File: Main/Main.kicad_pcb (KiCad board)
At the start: 2 copper layers, 55 parts, among them J1 Conn_02x16_Odd_Even, J2 TYPE-C 6P, Q3 S9013 J3(RANGE:200-350), U1 BQ24074RGT, U2 DRV8833PW, U3 HUSB237-AA001-DN06R, U4 RT9742GGJ5, U5 RT9742GGJ5, U6 INA219AxDCN, U7 TPS63802DLAR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

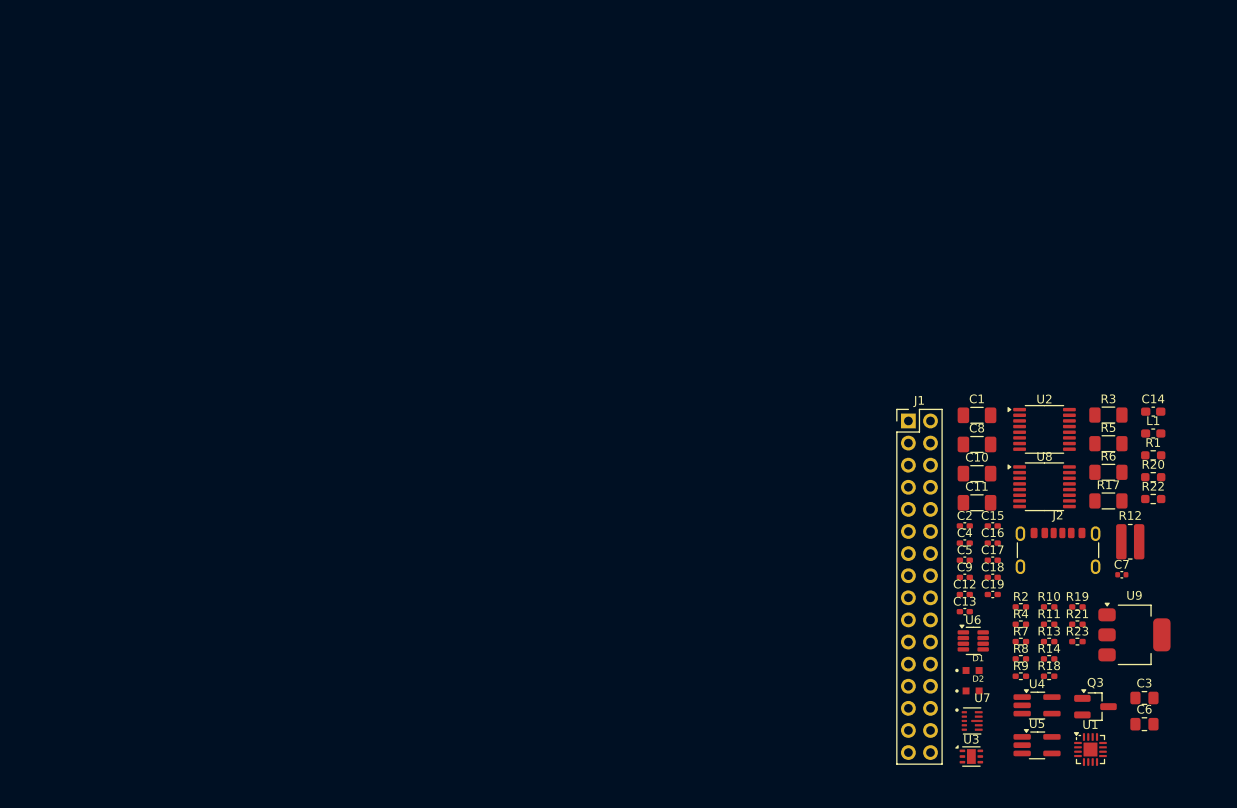
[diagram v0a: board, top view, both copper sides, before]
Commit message: Started PCB and Started Adding test points
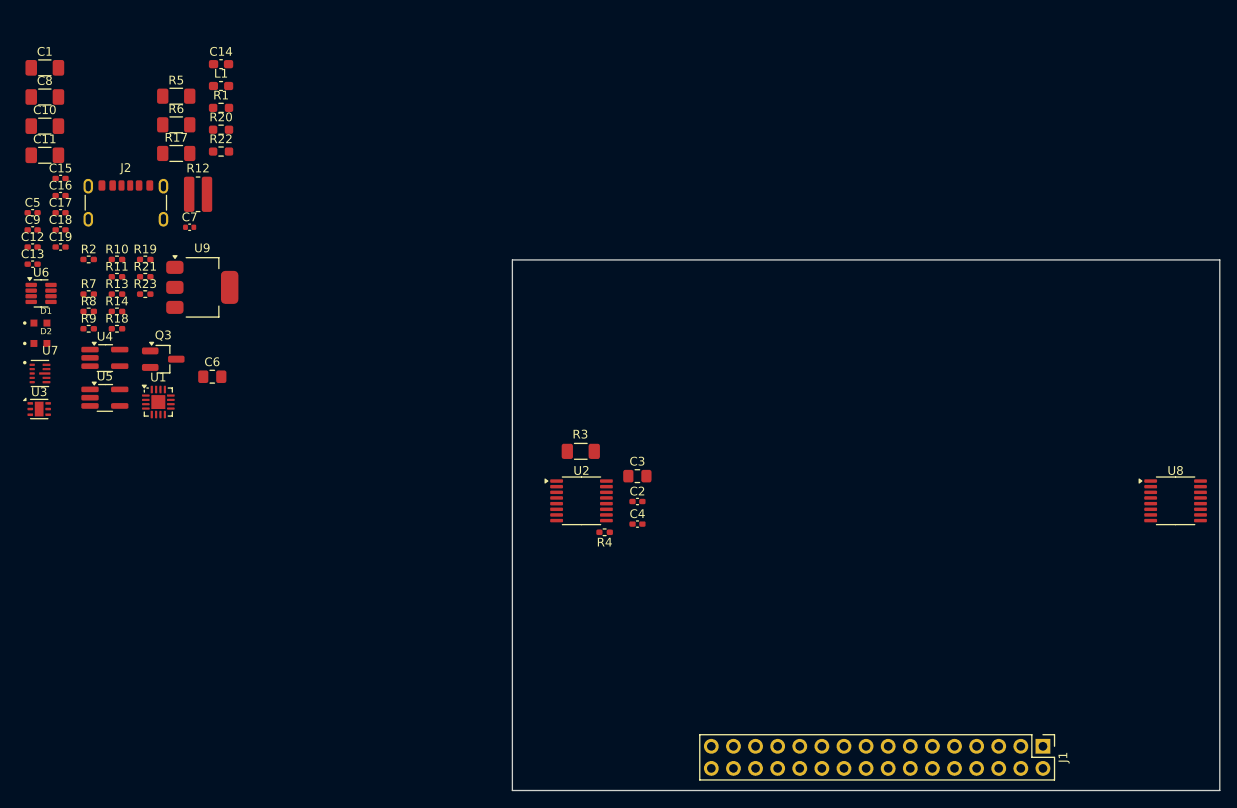
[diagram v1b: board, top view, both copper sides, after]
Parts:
- moved C1 114.3 mm to (40.3, 28.7)
- moved C10 114.3 mm to (40.3, 35.4)
- moved C11 114.3 mm to (40.3, 38.8)
- moved C14 114.3 mm to (60.5, 28.3)
- moved C15 114.3 mm to (42.1, 41.4)
- moved C16 114.3 mm to (42.1, 43.4)
- moved C17 114.3 mm to (42.1, 45.4)
- moved C18 114.3 mm to (42.1, 47.3)
- moved C19 114.3 mm to (42.1, 49.3)
- moved C8 114.3 mm to (40.3, 32.1)
- moved J2 114.3 mm to (49.6, 45.3)
- moved L1 114.3 mm to (60.5, 30.8)
- moved R1 114.3 mm to (60.5, 33.3)
- moved R20 114.3 mm to (60.5, 35.8)
- moved R22 114.3 mm to (60.5, 38.3)
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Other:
- board outline added: 81.3 x 61 mm

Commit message: connected first motor control
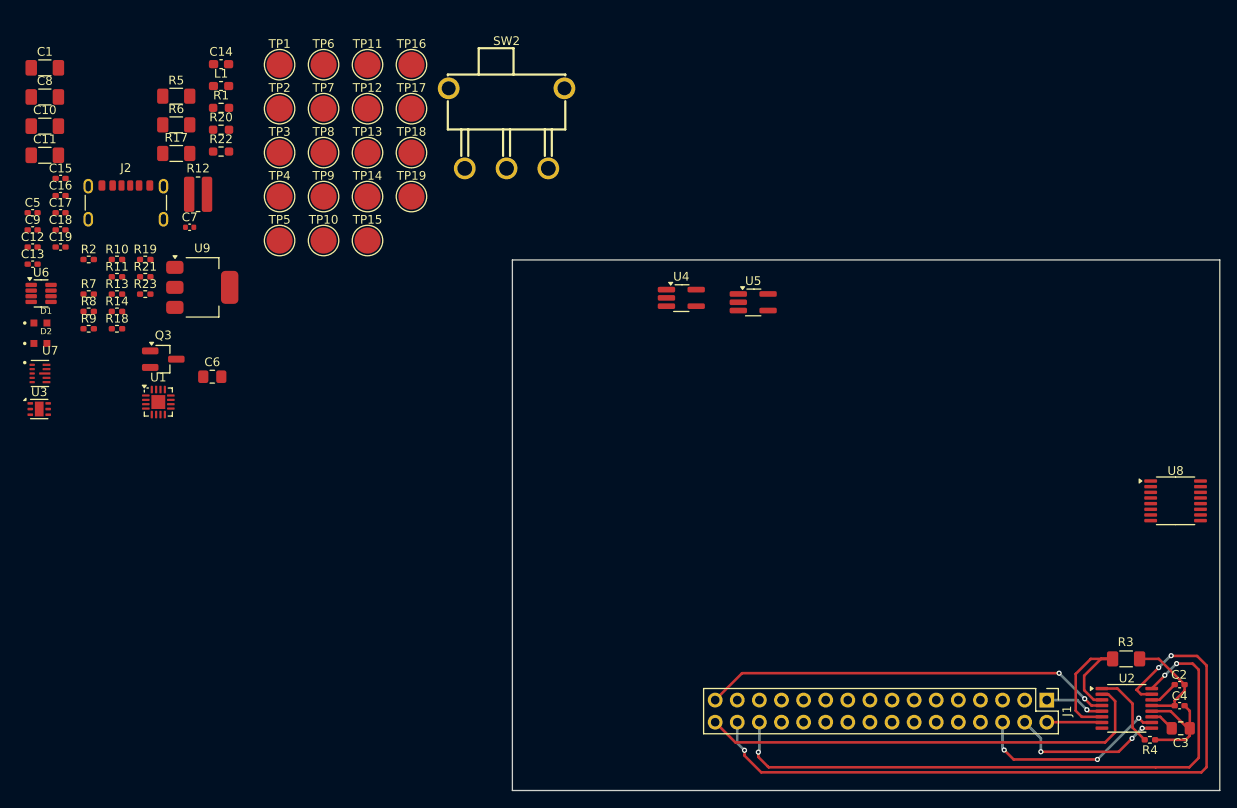
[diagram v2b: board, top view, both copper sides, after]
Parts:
- added SW2: SS-12D11G3R, SS-12D11G3R:SW-TH_SS-12D11L3, F.Cu at (93.3, 35.7)
- added TP1: TestPoint, TestPoint:TestPoint_Pad_D3.0mm, F.Cu at (67.2, 28.4)
- added TP10: TestPoint, TestPoint:TestPoint_Pad_D3.0mm, F.Cu at (72.3, 48.6)
- added TP11: TestPoint, TestPoint:TestPoint_Pad_D3.0mm, F.Cu at (77.3, 28.4)
- added TP12: TestPoint, TestPoint:TestPoint_Pad_D3.0mm, F.Cu at (77.3, 33.4)
- added TP13: TestPoint, TestPoint:TestPoint_Pad_D3.0mm, F.Cu at (77.3, 38.5)
- added TP14: TestPoint, TestPoint:TestPoint_Pad_D3.0mm, F.Cu at (77.3, 43.5)
- added TP15: TestPoint, TestPoint:TestPoint_Pad_D3.0mm, F.Cu at (77.3, 48.6)
- added TP16: TestPoint, TestPoint:TestPoint_Pad_D3.0mm, F.Cu at (82.4, 28.4)
- added TP17: TestPoint, TestPoint:TestPoint_Pad_D3.0mm, F.Cu at (82.4, 33.4)
- added TP18: TestPoint, TestPoint:TestPoint_Pad_D3.0mm, F.Cu at (82.4, 38.5)
- added TP19: TestPoint, TestPoint:TestPoint_Pad_D3.0mm, F.Cu at (82.4, 43.5)
- added TP2: TestPoint, TestPoint:TestPoint_Pad_D3.0mm, F.Cu at (67.2, 33.4)
- added TP3: TestPoint, TestPoint:TestPoint_Pad_D3.0mm, F.Cu at (67.2, 38.5)
- added TP4: TestPoint, TestPoint:TestPoint_Pad_D3.0mm, F.Cu at (67.2, 43.5)
- added TP5: TestPoint, TestPoint:TestPoint_Pad_D3.0mm, F.Cu at (67.2, 48.6)
- added TP6: TestPoint, TestPoint:TestPoint_Pad_D3.0mm, F.Cu at (72.3, 28.4)
- added TP7: TestPoint, TestPoint:TestPoint_Pad_D3.0mm, F.Cu at (72.3, 33.4)
- added TP8: TestPoint, TestPoint:TestPoint_Pad_D3.0mm, F.Cu at (72.3, 38.5)
- added TP9: TestPoint, TestPoint:TestPoint_Pad_D3.0mm, F.Cu at (72.3, 43.5)
- moved U5 75.3 mm to (121.7, 55.7)
- moved C3 68.8 mm to (170.8, 104.6), turned to 180 degrees
- moved U2 67.0 mm to (164.6, 102.3)
- moved R3 67.0 mm to (164.5, 96.6)
- moved R4 67.0 mm to (167.2, 105.9)
- moved U4 66.6 mm to (113.4, 55.2)
- moved C2 65.7 mm to (170.6, 99.6), turned to 180 degrees
- moved C4 65.7 mm to (170.6, 102.0), turned to 180 degrees
- moved J1 5.33 mm to (155.4, 101.4)
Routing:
- net /MOTOR1_CTRL2: track 0.00 -> 82.2 mm, vias 0 -> 3
- net /MOTOR1_CTRL1: track 0.00 -> 72.6 mm, vias 0 -> 3
- net /MOTOR1_A_OUT: track 0.00 -> 52.8 mm
- net /MOTOR1_B_OUT: track 0.00 -> 47.4 mm, vias 0 -> 2
- net /MOTOR2_CTRL2: track 0.00 -> 23.0 mm, vias 0 -> 3
- net Net-(U2-AISEN): track 0.00 -> 20.7 mm
- net /MOTOR2_CTRL1: track 0.00 -> 18.1 mm, vias 0 -> 3
- net /3V3 Out: track 0.00 -> 13.1 mm
- net GND: track 0.00 -> 12.0 mm
- net Net-(U2-~{SLEEP}): track 0.00 -> 8.98 mm
- net /Motor2_B_OUT: track 0.00 -> 6.86 mm, vias 0 -> 1
- net /Motor2_A_OUT: track 0.00 -> 6.35 mm
- net Net-(U2-VINT): track 0.00 -> 3.36 mm
- net Net-(U2-VCP): track 0.00 -> 2.84 mm

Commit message: Completed substantial PCB Connections
Completed: 1A Switching, Charging IC
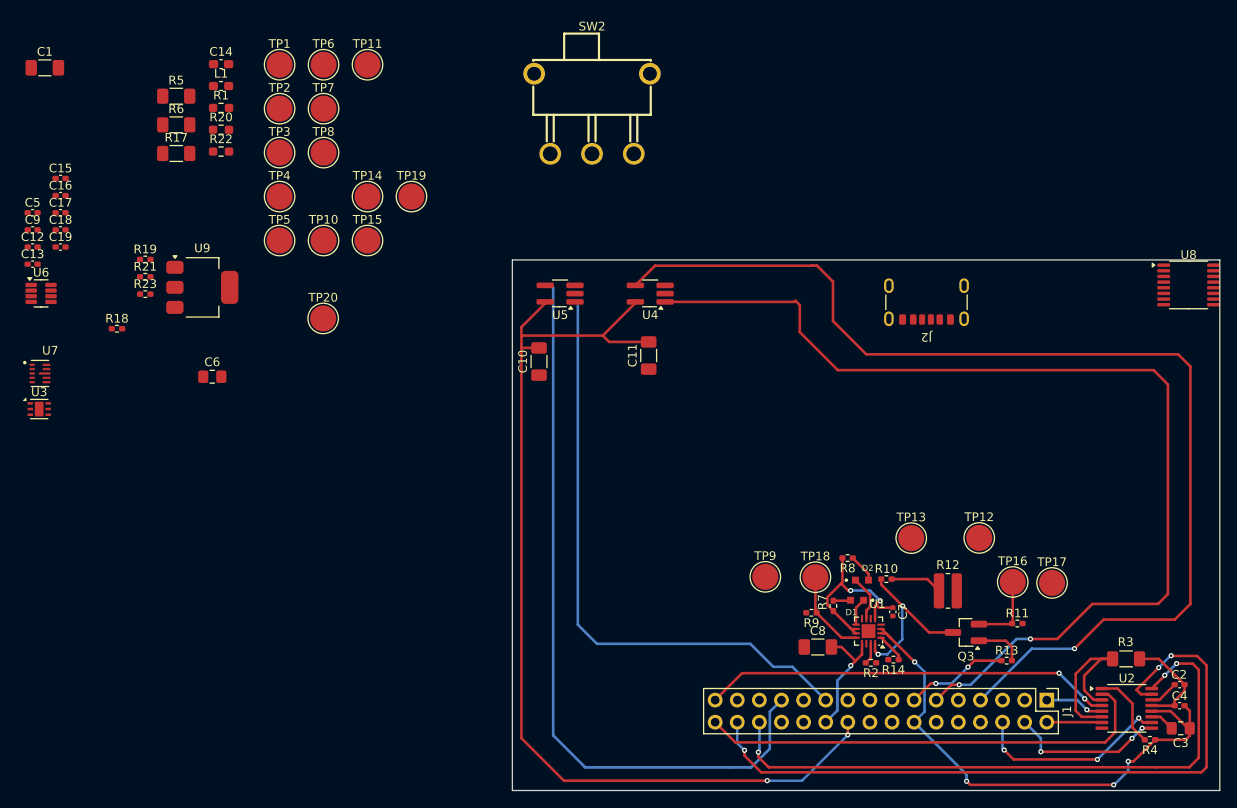
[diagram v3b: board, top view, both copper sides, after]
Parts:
- added TP20: TestPoint, TestPoint:TestPoint_Pad_D3.0mm, F.Cu at (72.2, 57.5)
- moved R11 110.9 mm to (152.0, 92.6)
- moved R13 110.6 mm to (150.8, 96.8)
- moved C8 109.0 mm to (129.1, 95.3)
- moved R2 101.1 mm to (135.2, 97.1), turned to 180 degrees
- moved D1 99.1 mm to (133.6, 89.9), turned to 180 degrees
- moved D2 98.2 mm to (134.2, 87.6)
- moved R14 97.8 mm to (137.8, 96.7), turned to 180 degrees
- moved R12 97.5 mm to (144.0, 88.8)
- moved Q3 97.4 mm to (146.1, 93.6), turned to 180 degrees
- moved R10 95.7 mm to (137.0, 87.5)
- moved R7 92.8 mm to (130.9, 90.5), turned to -90 degrees
- moved J2 92.5 mm to (141.6, 54.6), turned to 180 degrees
- moved C7 92.1 mm to (137.7, 91.2), turned to -90 degrees
- moved R8 91.7 mm to (132.5, 85.0), turned to 180 degrees
- moved TP17 91.6 mm to (156.0, 87.9)
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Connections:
- C18 pad 1: /3V3 Out -> /Battery
- C3 pad 1: /3V3 Out -> /Battery
- C4 pad 1: /3V3 Out -> /Battery
- C6 pad 1: /3V3 Out -> /Battery
- R19 pad 1: /3V3 Out -> /Battery
- R4 pad 1: /3V3 Out -> /Battery
- U2 pad 12: /3V3 Out -> /Battery
- U8 pad 12: /3V3 Out -> /Battery
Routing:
- net /CTRL_EXT_LOAD2: track 0.00 -> 128.2 mm, vias 0 -> 1
- net /EXT_LOAD2_OUT: track 0.00 -> 119.4 mm, vias 0 -> 2
- net /5V Out: track 0.00 -> 116.8 mm, vias 0 -> 2
- net /CTRL_EXT_LOAD1: track 0.00 -> 84.9 mm
- net /EXT_LOAD1_OUT: track 0.00 -> 68.9 mm
- net /Battery: track 0.00 -> 61.8 mm, vias 0 -> 4
- net /VOUT: track 0.00 -> 21.1 mm, vias 0 -> 2
- net Net-(Q3-C): track 0.00 -> 19.9 mm, vias 0 -> 2
- net /High Voltage (9V): track 0.00 -> 14.3 mm, vias 0 -> 1
- net /3V3 Out: track 13.1 -> 0.00 mm
- net /FAST_CHARGE_CTRL: track 0.00 -> 11.9 mm, vias 0 -> 2
- net Net-(U1-ILIM): track 0.00 -> 9.86 mm
- net Net-(Q3-E): track 0.00 -> 8.64 mm
- net Net-(R10-Pad2): track 0.00 -> 6.00 mm
- net Net-(Q3-B): track 0.00 -> 5.66 mm
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
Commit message: Finished 9V implementation and PD system
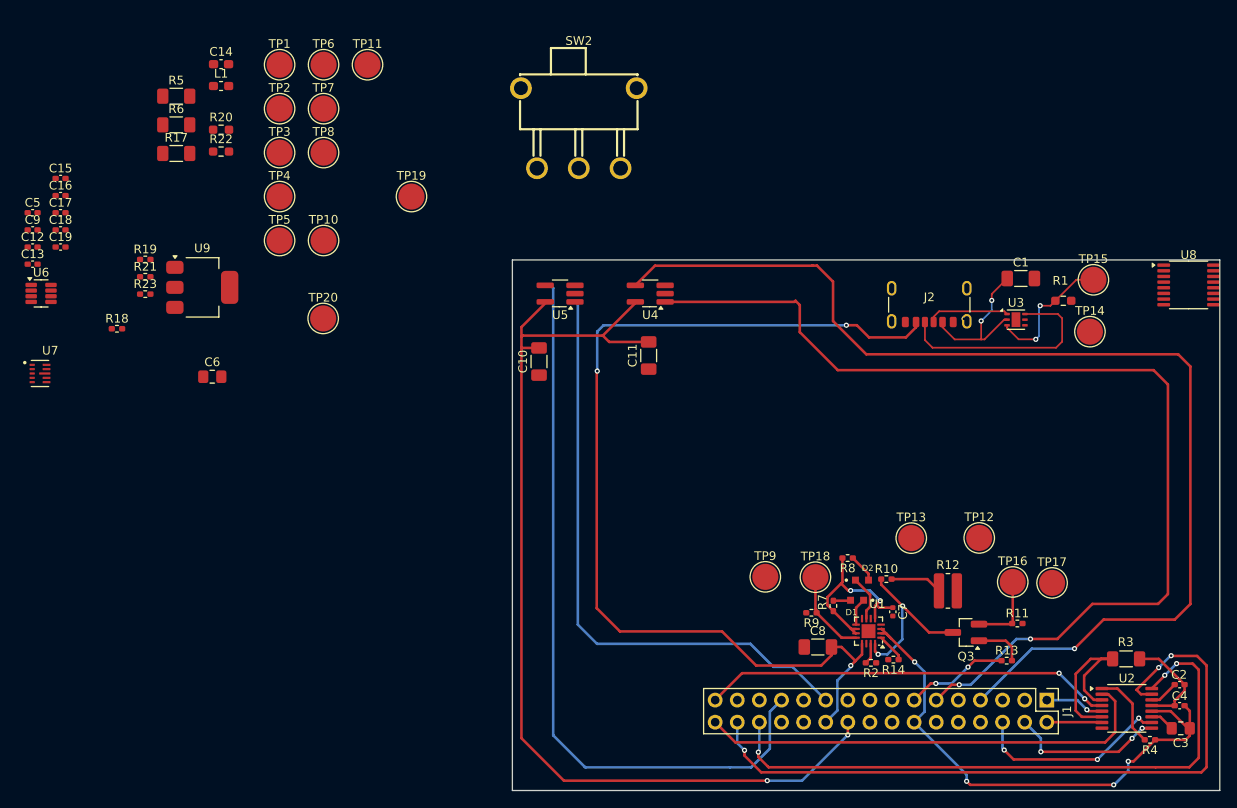
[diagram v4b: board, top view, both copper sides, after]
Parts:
- moved C1 114.7 mm to (152.4, 52.9)
- moved U3 112.7 mm to (151.8, 57.7)
- moved R1 99.3 mm to (157.3, 55.5)
- moved TP14 84.4 mm to (160.3, 59.0)
- moved TP15 83.5 mm to (160.7, 53.1)
- moved SW2 2.25 mm to (101.6, 35.7)
- moved J2 0.43 mm to (141.9, 54.9)
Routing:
- net /High Voltage (9V): track 14.3 -> 133.9 mm, vias 1 -> 5
- net Net-(J2-CC2): track 0.00 -> 25.6 mm
- net Net-(U3-VSET): track 0.00 -> 15.6 mm, vias 0 -> 2
- net Net-(J2-CC1): track 0.00 -> 9.43 mm
- net (no net): vias 0 -> 1

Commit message: Added the Switch and Connected the Battery pin to it
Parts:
- moved SW2 42.8 mm to (116.2, 75.9)
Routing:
- net /Battery: track 61.8 -> 104.3 mm
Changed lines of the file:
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@@
 	(footprint "SS-12D11G3R:SW-TH_SS-12D11L3"
 		(layer "F.Cu")
-		(at 101.61 35.66)
+		(at 116.23 75.9)
 		(property "Reference" "SW2"
 			(at 0 -10.037 0)
@@
 	)
 	(segment
+		(start 141.341 98.131)
+		(end 141.341 102.709)
+		(width 0.3)
+		(layer "B.Cu")
+		(net 9)
+	)
+	(segment
+		(start 140.2 96.99)
+		(end 140.755 97.545)
+		(width 0.3)
+		(layer "B.Cu")
+		(net 9)
+	)
+	(segment
 		(start 163.07 111.109)
 		(end 163.01 111.109)
@@
 	)
 	(segment
-		(start 141.341 98.131)
-		(end 141.341 102.709)
+		(start 141.341 102.709)
+		(end 140.14 103.91)
 		(width 0.3)
 		(layer "B.Cu")
@@
 	)
 	(segment
+		(start 140.755 97.545)
+		(end 141.53 96.77)
+		(width 0.5)
+		(layer "B.Cu")
+		(net 9)
+	)
+	(segment
+		(start 141.53 88.88)
+		(end 136.7 84.05)
+		(width 0.5)
+		(layer "B.Cu")
+		(net 9)
+	)
+	(segment
 		(start 146.17 110.7)
 		(end 146.17 109.94)
@@
 	)
 	(segment
-		(start 141.341 102.709)
-		(end 140.14 103.91)
-		(width 0.3)
+		(start 114.98 84.05)
+		(end 111.43 80.5)
+		(width 0.5)
 		(layer "B.Cu")
 		(net 9)
 	)
 	(segment
-		(start 140.2 96.99)
+		(start 141.53 96.77)
+		(end 141.53 88.88)
+		(width 0.5)
+		(layer "B.Cu")
+		(net 9)
+	)
+	(segment
+		(start 136.7 84.05)
+		(end 114.98 84.05)
+		(width 0.5)
+		(layer "B.Cu")
+		(net 9)
+	)
+	(segment
+		(start 140.755 97.545)
 		(end 141.341 98.131)
 		(width 0.3)

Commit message: Removed the GND for one of the motor ICs
Pouring ground so ground not connected
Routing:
- net GND: track 12.0 -> 0.08 mm
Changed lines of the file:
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@@
-	)
-	(segment
-		(start 171.212444 100.2975)
-		(end 170.077444 101.4325)
-		(width 0.3)
-		(layer "F.Cu")
-		(net 1)
-	)
-	(segment
-		(start 168.252444 96.635)
-		(end 171.212444 99.595)
-		(width 0.3)
-		(layer "F.Cu")
-		(net 1)
 	)
 	(segment
@@
 	)
 	(segment
-		(start 170.077444 102.015)
-		(end 167.459944 102.015)
-		(width 0.3)
-		(layer "F.Cu")
-		(net 1)
-	)
-	(segment
-		(start 170.077444 101.4325)
-		(end 170.077444 102.015)
-		(width 0.3)
-		(layer "F.Cu")
-		(net 1)
-	)
-	(segment
-		(start 171.212444 99.595)
-		(end 171.212444 100.2975)
-		(width 0.3)
-		(layer "F.Cu")
-		(net 1)
-	)
-	(segment
 		(start 167.459944 102.015)
 		(end 167.439944 101.995)
 		(width 0.3)
 		(layer "F.Cu")
-		(net 1)
-	)
-	(segment
-		(start 166.044944 96.635)
-		(end 168.252444 96.635)
-		(width 0.3)
-		(layer "F.Cu")

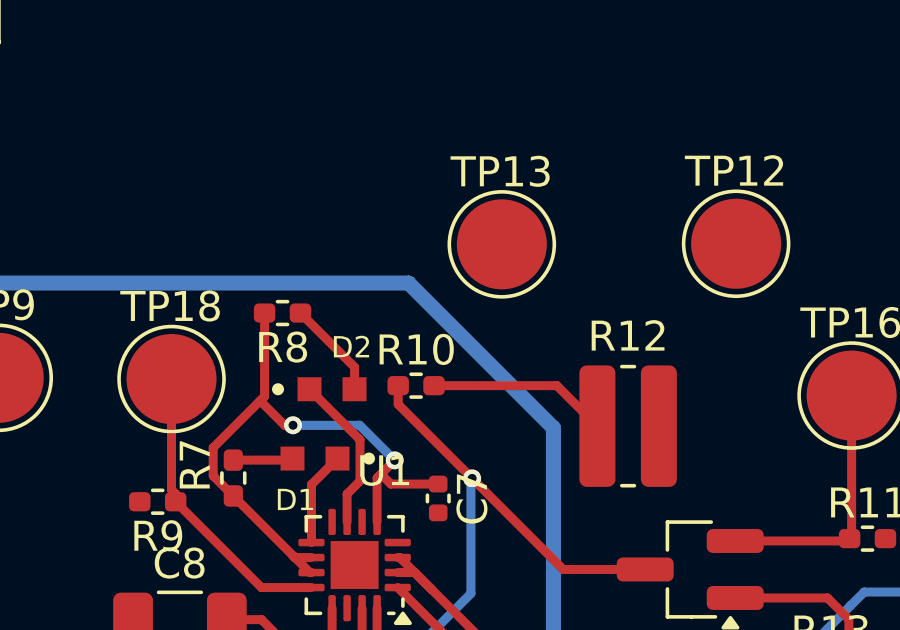
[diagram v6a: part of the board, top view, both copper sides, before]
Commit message: PB-13 was unconnected - it is now connected
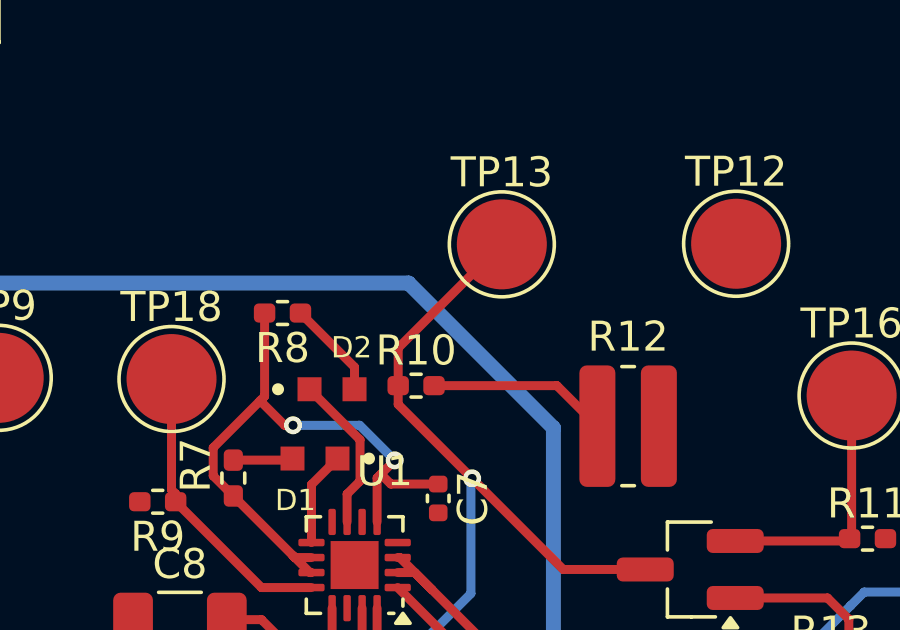
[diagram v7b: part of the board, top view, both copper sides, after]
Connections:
- TP13 pad 1: unconnected-(TP13-Pad1) -> Net-(Q3-C)
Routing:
- net Net-(Q3-C): track 19.9 -> 26.0 mm
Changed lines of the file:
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@@
 	(net 69 "unconnected-(SW2-Pad4)")
 	(net 70 "unconnected-(SW2-Pad5)")
-	(net 71 "unconnected-(TP13-Pad1)")
 	(footprint "Package_SO:TSSOP-16_4.4x5mm_P0.65mm"
 		(layer "F.Cu")
@@
 			(size 3 3)
 			(layers "F.Cu" "F.Mask")
-			(net 71 "unconnected-(TP13-Pad1)")
+			(net 46 "Net-(Q3-C)")
 			(pinfunction "1")
 			(pintype "passive")
@@
 	)
 	(segment
+		(start 136.355 86.215)
+		(end 136.355 87.47)
+		(width 0.3)
+		(layer "F.Cu")
+		(net 46)
+	)
+	(segment
 		(start 135.6525 94.8875)
 		(end 135.6525 95.7625)
 		(width 0.3)
 		(layer "F.Cu")
+		(net 46)
+	)
+	(segment
+		(start 139.81 82.76)
+		(end 136.355 86.215)
+		(width 0.3)
+		(layer "F.Cu")
